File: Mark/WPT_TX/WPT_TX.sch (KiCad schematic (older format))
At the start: 119 parts, among them J1 Conn_01x01, J10 Conn_01x01, J2 Conn_01x01, J3 Conn_Coaxial, J4 Conn_Coaxial, J5 Conn_Coaxial, J6 Conn_02x05_Odd_Even, J7 Conn_01x03, J8 Conn_01x04, J9 Conn_01x01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

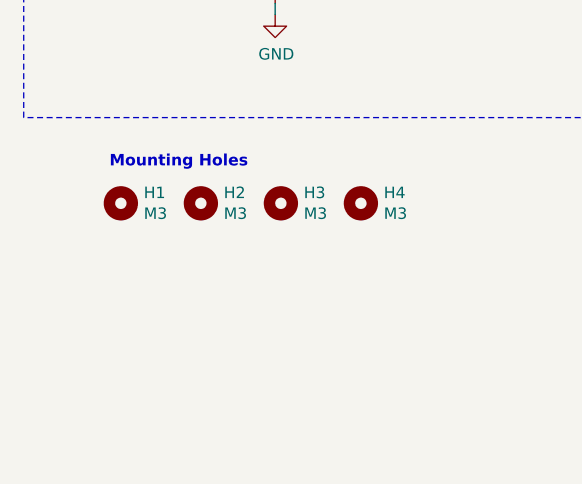
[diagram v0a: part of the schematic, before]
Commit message: Silkscreen & Touchups
- Board is finished!
- Fixed up silkscreen and some placement, looks good.
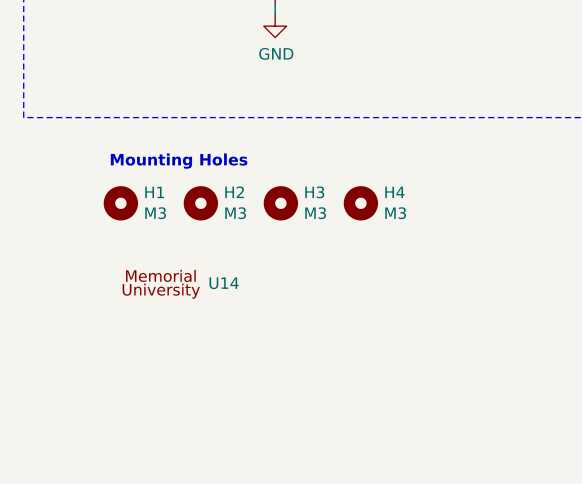
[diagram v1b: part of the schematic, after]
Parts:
- added U14: Munlogo, WPT_TX:MUNLOGO, symbol WPT_TX:Munlogo
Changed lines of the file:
@@
 	-1   0    0    1
 $EndComp
+$Comp
+L WPT_TX:Munlogo U14
+U 1 1 5FB55A13
+P 1175 10150
+F 0 "U14" H 1382 10149 50  0000 L CNN
+F 1 "Munlogo" H 1185 10040 50  0001 C CNN
+F 2 "WPT_TX:MUNLOGO" H 1175 10240 50  0001 C CNN
+F 3 "" H 1175 10240 50  0001 C CNN
+	1    1175 10150
+	1    0    0    -1
+$EndComp
 $EndSCHEMATC

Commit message: Updated TX
- Changed OL detector to a non inverting schmitt trigger.
- Updated routing, added more vias
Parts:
- added R26: 10k, Resistor_SMD:R_0603_1608Metric, symbol WPT_TX-rescue:R_US-Device
- R2: value 79.6k -> 10k; Digikey 13-RT0603BRD0779K6LCT-ND -> RHM10KDCT-ND
- R3: value 10k -> 12k; Digikey RHM10KDCT-ND -> P12KDBCT-ND
- R5: value 79.6k -> 1k; Digikey 13-RT0603BRD0779K6LCT-ND -> RHM1.0KDCT-ND
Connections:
- net ISEN: now also R5.2; no longer U5.2 (-)
- net at R7.2, U5.1, U6.4 (S1): now also R26.1; no longer R5.2
- net at R5.1, U5.3 (+): now also R26.2; no longer R2.1, R3.2
- new net VREF: R2.1, R3.2, U5.2 (-)
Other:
- moved on the sheet: C1, C10, C11, C12, C13, C14, C15, C16, C17, C18, C19, C2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

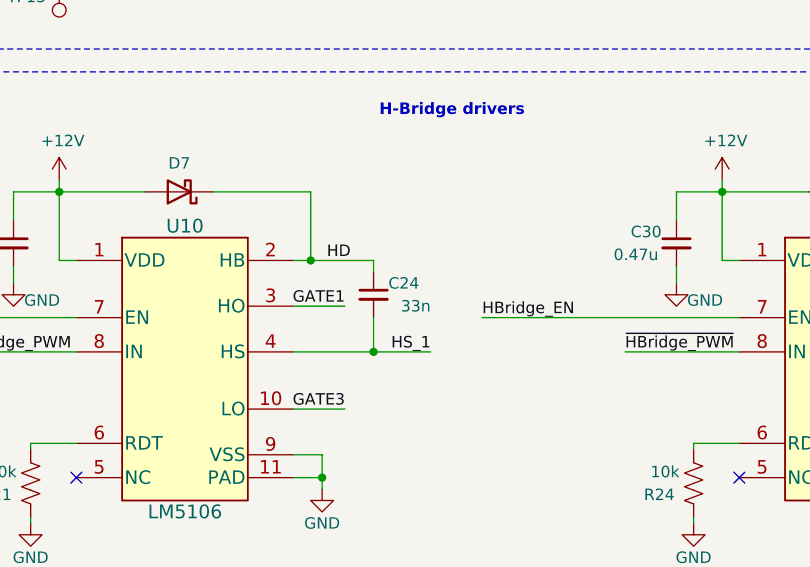
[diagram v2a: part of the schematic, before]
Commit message: Gerbers
- Generated gerbers
- Changed TX board size to 45x100mm to match RX board.
- Ordered PCBs like the impaitent bastard I am
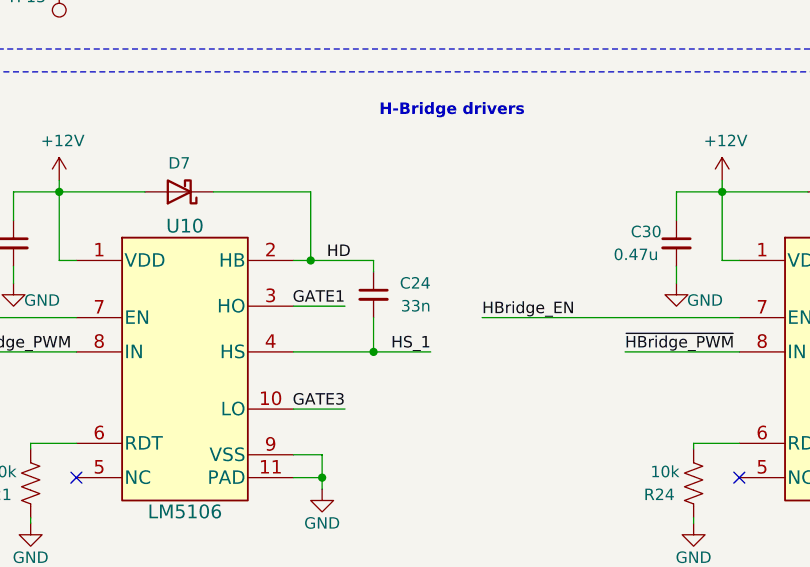
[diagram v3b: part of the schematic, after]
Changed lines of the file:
@@
 U 1 1 61B822E7
 P 11875 4125
-F 0 "C24" H 11675 4175 50  0000 L CNN
+F 0 "C24" H 11625 4175 50  0000 L CNN
 F 1 "33n" H 11625 4075 50  0000 L CNN
 F 2 "Capacitor_SMD:C_0805_2012Metric" H 11875 4125 50  0001 C CNN
